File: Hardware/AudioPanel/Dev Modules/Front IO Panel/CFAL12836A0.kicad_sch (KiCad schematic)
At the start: 16 parts, among them U201 CFAL12836A0

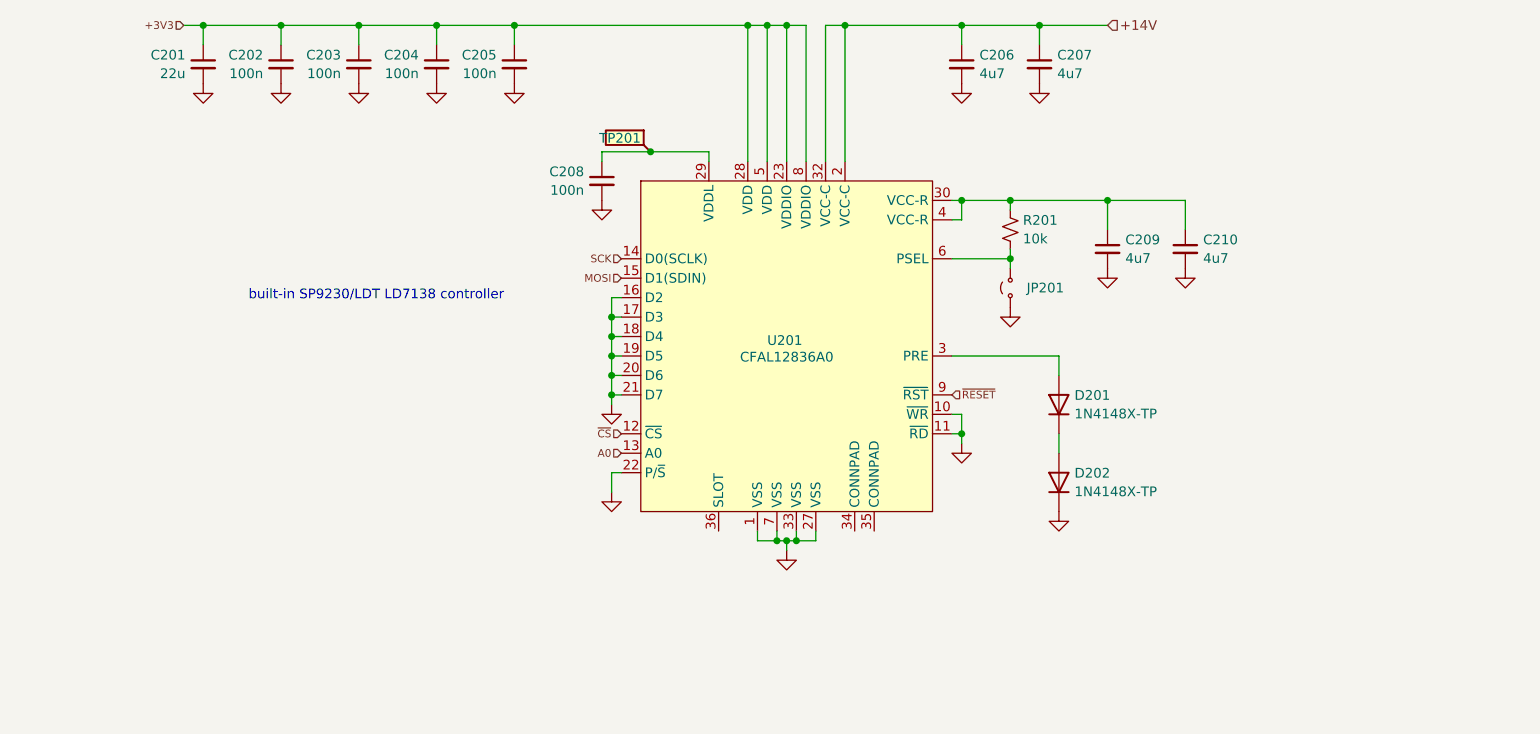
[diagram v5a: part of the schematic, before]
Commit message: Reorganized PISO bits
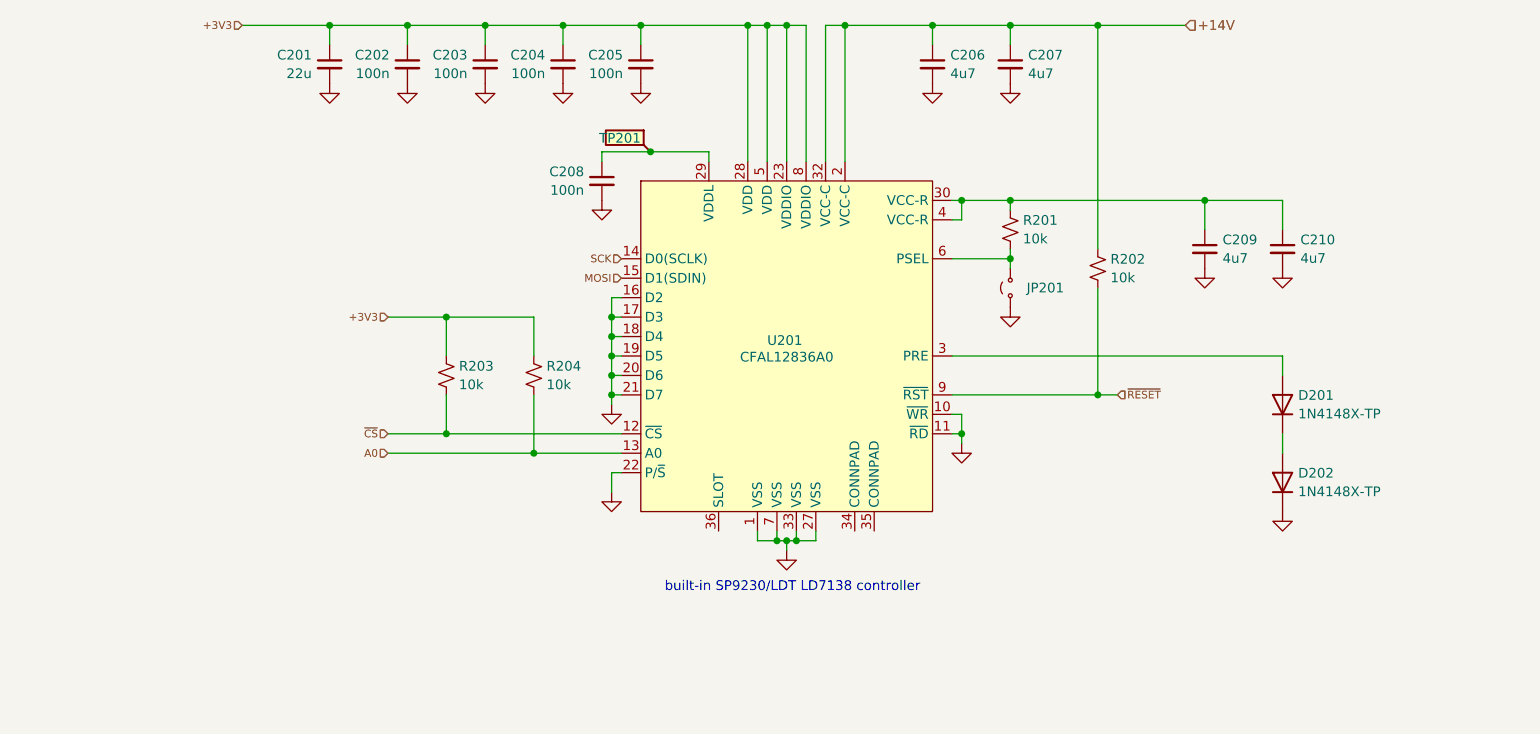
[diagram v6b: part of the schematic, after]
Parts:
- added R202, R203, R204: 10k, Libraries:Worthington_R_0402, symbol Device:R_Small_US
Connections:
- net +14V: now also R202.1
- net +3V3: now also R203.1, R204.1
- net A0: now also R204.2
- net ~{CS}: now also R203.2
- net ~{RESET}: now also R202.2
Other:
- moved on the sheet: C201, C202, C203, C204, C205, C206, C207, C209, C210, D201, D202

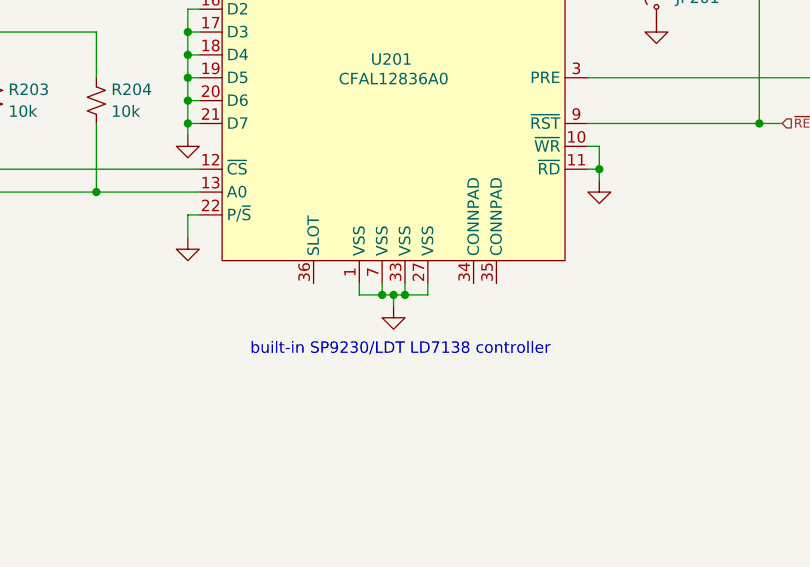
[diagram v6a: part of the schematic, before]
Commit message: Fixed footprint errors, placed onto PCBs
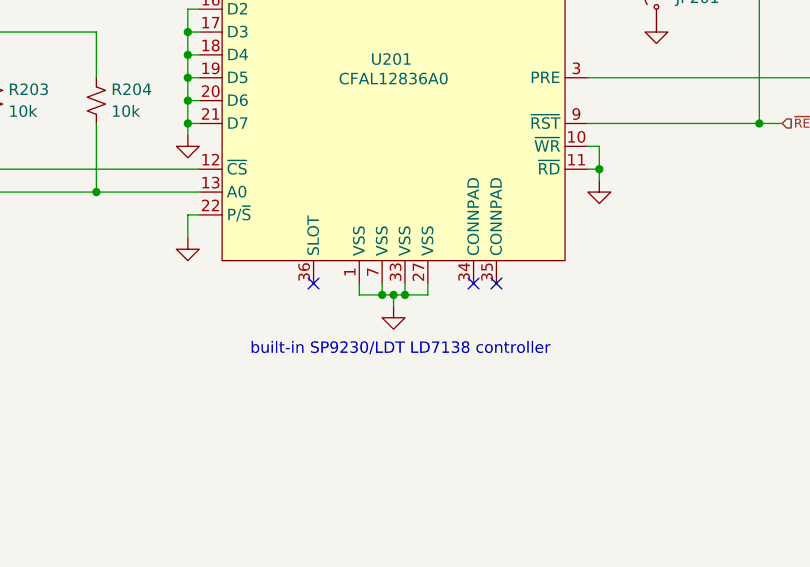
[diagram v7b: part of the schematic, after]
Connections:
- no-connect marks 0 -> 3
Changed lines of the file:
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@@
 		(color 0 0 0 0)
+	)
+	(no_connect
+		(at 227.33 162.56)
+	)
+	(no_connect
+		(at 207.01 162.56)
+	)
+	(no_connect
+		(at 224.79 162.56)
 	)
 	(wire
